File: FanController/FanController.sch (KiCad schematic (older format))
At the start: 16 parts, among them J1 Conn_01x02, J2 Conn_01x02, J3 Conn_01x02, Q1 BTA16, U1 MOC3020, U2 EL817, U3 NodeMCU1.0(ESP-12E)

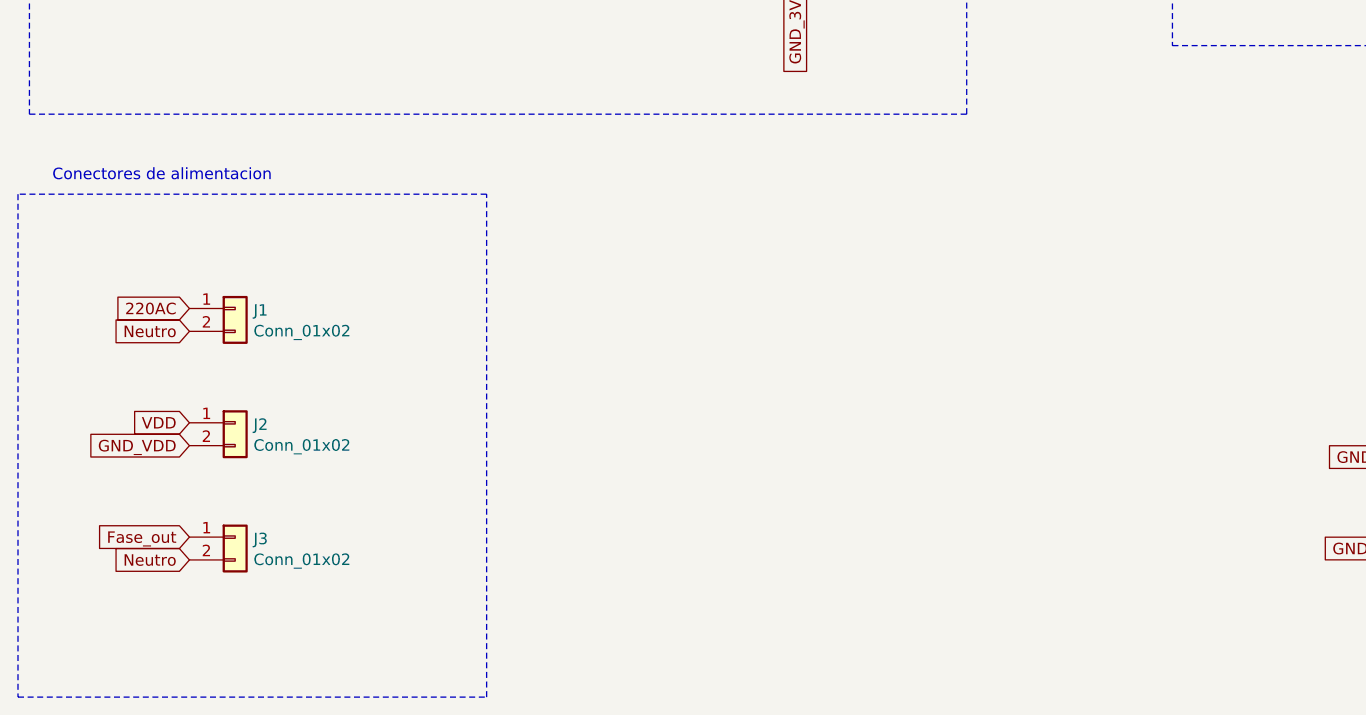
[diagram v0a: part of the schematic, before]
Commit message: added in schematic ASDC suplier for ESP12E.
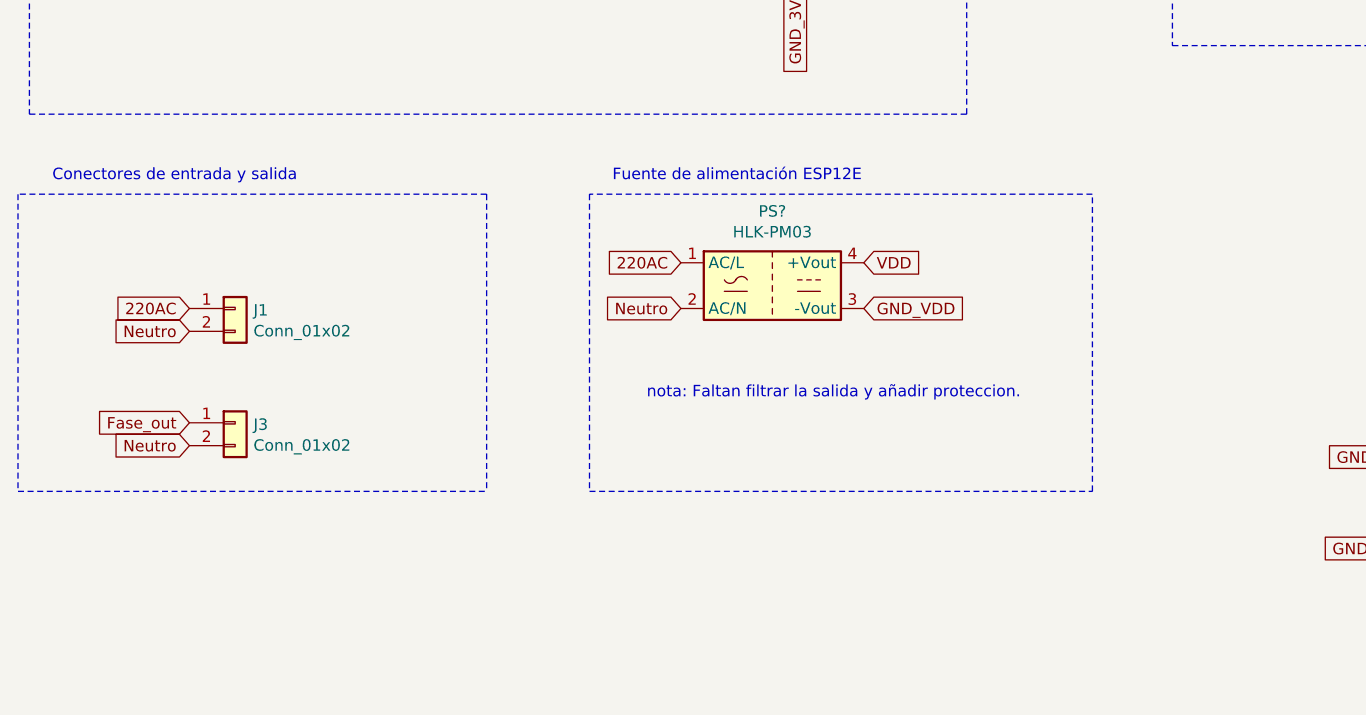
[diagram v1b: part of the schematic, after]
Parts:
- removed J2: Conn_01x02, TerminalBlock_Phoenix:TerminalBlock_Phoenix_MKDS-1,5-2_1x02_P5.00mm_Horizontal, symbol Connector_Generic:Conn_01x02
- added PS?: HLK-PM03, Converter_ACDC:Converter_ACDC_HiLink_HLK-PMxx, symbol Converter_ACDC:HLK-PM03
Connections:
- net 220AC: now also PS?.1 (AC/L)
- net GND_VDD: now also PS?.3 (-Vout)
- net Neutro: now also PS?.2 (AC/N)
- net VDD: now also PS?.4 (+Vout)
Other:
- note added: "Conectores de entrada y salida\n"
- note added: "Fuente de alimentación ESP12E\n"
- note added: "nota: Faltan filtrar la salida y añadir proteccion."
- note removed: "Conectores de alimentacion\n"
- moved on the sheet: J3
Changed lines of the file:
@@
 Comment4 ""
 $EndDescr
-Wire Notes Line
-	1350 4050 1350 6250
 Text Notes 1500 4000 0    50   ~ 0
-Conectores de alimentacion\n
+Conectores de entrada y salida\n
 Text GLabel 2000 1800 0    50   Input ~ 0
 220AC
@@
 L Connector_Generic:Conn_01x02 J3
 U 1 1 5EDAB3AB
-P 2300 5550
-F 0 "J3" H 2380 5542 50  0000 L CNN
-F 1 "Conn_01x02" H 2380 5451 50  0000 L CNN
-F 2 "TerminalBlock_Phoenix:TerminalBlock_Phoenix_MKDS-1,5-2_1x02_P5.00mm_Horizontal" H 2300 5550 50  0001 C CNN
-F 3 "~" H 2300 5550 50  0001 C CNN
-	1    2300 5550
-	1    0    0    -1
-$EndComp
-Text GLabel 2100 5650 0    50   Input ~ 0
+P 2300 5050
+F 0 "J3" H 2380 5042 50  0000 L CNN
+F 1 "Conn_01x02" H 2380 4951 50  0000 L CNN
+F 2 "TerminalBlock_Phoenix:TerminalBlock_Phoenix_MKDS-1,5-2_1x02_P5.00mm_Horizontal" H 2300 5050 50  0001 C CNN
+F 3 "~" H 2300 5050 50  0001 C CNN
+	1    2300 5050
+	1    0    0    -1
+$EndComp
+Text GLabel 2100 5150 0    50   Input ~ 0
 Neutro
-Text GLabel 2100 5550 0    50   Input ~ 0
+Text GLabel 2100 5050 0    50   Input ~ 0
 Fase_out
 $Comp
@@
 NoConn ~ 7500 5000
 NoConn ~ 7500 5100
-$Comp
-L Connector_Generic:Conn_01x02 J2
-U 1 1 5ECAE5DF
-P 2300 5050
-F 0 "J2" H 2380 5042 50  0000 L CNN
-F 1 "Conn_01x02" H 2380 4951 50  0000 L CNN
-F 2 "TerminalBlock_Phoenix:TerminalBlock_Phoenix_MKDS-1,5-2_1x02_P5.00mm_Horizontal" H 2300 5050 50  0001 C CNN
-F 3 "~" H 2300 5050 50  0001 C CNN
-	1    2300 5050
-	1    0    0    -1
-$EndComp
-Text GLabel 2100 5050 0    50   Input ~ 0
+Text GLabel 5050 4350 2    50   Input ~ 0
 VDD
-Text GLabel 2100 5150 0    50   Input ~ 0
+Text GLabel 5050 4550 2    50   Input ~ 0
 GND_VDD
 Text GLabel 7500 5700 0    50   Input ~ 0
@@
 GND_VDD
 Wire Notes Line
-	1350 6250 3400 6250
-Wire Notes Line
-	3400 6250 3400 4050
+	1350 5350 3400 5350
 Wire Notes Line
 	3400 4050 1350 4050
+$Comp
+L Converter_ACDC:HLK-PM03 PS?
+U 1 1 5F2C88CC
+P 4650 4450
+F 0 "PS?" H 4650 4775 50  0000 C CNN
+F 1 "HLK-PM03" H 4650 4684 50  0000 C CNN
+F 2 "Converter_ACDC:Converter_ACDC_HiLink_HLK-PMxx" H 4650 4150 50  0001 C CNN
+F 3 "http://www.hlktech.net/product_detail.php?ProId=59" H 5050 4100 50  0001 C CNN
+	1    4650 4450
+	1    0    0    -1
+$EndComp
+Text GLabel 4250 4350 0    50   Input ~ 0
+220AC
+Text GLabel 4250 4550 0    50   Input ~ 0
+Neutro
+Wire Notes Line
+	3400 4050 3400 5350
+Wire Notes Line
+	3850 4050 3850 5350
+Wire Notes Line
+	3850 5350 6050 5350
+Wire Notes Line
+	6050 5350 6050 4050
+Wire Notes Line
+	6050 4050 3850 4050
+Text Notes 3950 4000 0    50   ~ 0
+Fuente de alimentación ESP12E\n
+Text Notes 4100 4950 0    50   ~ 0
+nota: Faltan filtrar la salida y añadir proteccion.
+Wire Notes Line
+	1350 4050 1350 5350
 $EndSCHEMATC

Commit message: added capacitor network at the output of ACDC
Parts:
- added C1: 10uf, Capacitor_THT:C_Rect_L31.5mm_W13.0mm_P27.50mm_MKS4, symbol Device:CP
- added C2: 22uf, Capacitor_THT:C_Rect_L31.5mm_W13.0mm_P27.50mm_MKS4, symbol Device:CP
- gave numbers to parts that had none: 1
- renumbered J3 to J2
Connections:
- net 220AC: now also R1.1; no longer J1.1 (Pin_1)
- net at F1.1: now also J1.1 (Pin_1); no longer R1.1
- net GND_VDD renamed +3V3
- net +3V3: now also PS1.4 (+Vout), C1.1, C2.1; no longer PS1.3 (-Vout)
- net VDD renamed GND
- net GND: now also PS1.3 (-Vout), C1.2, C2.2; no longer PS1.4 (+Vout)
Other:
- note added: "nota: se podría añadir un fusible para proteger el uC\n\n"
- note removed: "nota: Faltan filtrar la salida y añadir proteccion."
- moved on the sheet: F1, J1, J2, R4, RV1
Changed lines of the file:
@@
 Text Notes 1500 4000 0    50   ~ 0
 Conectores de entrada y salida\n
-Text GLabel 2000 1800 0    50   Input ~ 0
-220AC
-Text GLabel 2000 2250 0    50   Input ~ 0
-Neutro
 $Comp
 L Device:R R1
@@
 L Device:R R4
 U 1 1 5ECD0D61
-P 2150 2450
-F 0 "R4" H 2220 2496 50  0000 L CNN
-F 1 "47K" H 2220 2405 50  0000 L CNN
-F 2 "Resistor_THT:R_Axial_DIN0207_L6.3mm_D2.5mm_P10.16mm_Horizontal" V 2080 2450 50  0001 C CNN
-F 3 "~" H 2150 2450 50  0001 C CNN
-	1    2150 2450
-	1    0    0    -1
-$EndComp
-Wire Wire Line
-	3250 2600 2150 2600
+P 2300 2450
+F 0 "R4" H 2370 2496 50  0000 L CNN
+F 1 "47K" H 2370 2405 50  0000 L CNN
+F 2 "Resistor_THT:R_Axial_DIN0207_L6.3mm_D2.5mm_P10.16mm_Horizontal" V 2230 2450 50  0001 C CNN
+F 3 "~" H 2300 2450 50  0001 C CNN
+	1    2300 2450
+	1    0    0    -1
+$EndComp
 $Comp
 L Device:R R5
@@
 Wire Wire Line
 	4750 3100 4750 2950
-Wire Notes Line
-	1400 1200 1400 3700
-Wire Notes Line
-	1400 3700 5500 3700
-Wire Notes Line
-	5500 3700 5500 1200
-Wire Notes Line
-	5500 1200 1400 1200
-Text Notes 1450 1150 0    50   ~ 0
+Text Notes 1400 950  0    50   ~ 0
 Entrada AC y conversion a sinosoudal de baja tensión\n
 Wire Wire Line
@@
 $EndComp
 Wire Wire Line
-	2000 1800 2150 1800
-Wire Wire Line
 	4600 2650 4750 2650
 Connection ~ 4750 2650
@@
 L Device:Varistor RV1
 U 1 1 5ED798EB
-P 2150 2000
-F 0 "RV1" H 2253 2046 50  0000 L CNN
-F 1 "Varistor" H 2253 1955 50  0000 L CNN
-F 2 "Varistor:RV_Disc_D7mm_W3.4mm_P5mm" V 2080 2000 50  0001 C CNN
-F 3 "~" H 2150 2000 50  0001 C CNN
-	1    2150 2000
-	1    0    0    -1
-$EndComp
-Wire Wire Line
-	2150 1800 2150 1850
+P 2300 1850
+F 0 "RV1" H 2403 1896 50  0000 L CNN
+F 1 "Varistor" H 2403 1805 50  0000 L CNN
+F 2 "Varistor:RV_Disc_D7mm_W3.4mm_P5mm" V 2230 1850 50  0001 C CNN
+F 3 "~" H 2300 1850 50  0001 C CNN
+	1    2300 1850
+	1    0    0    -1
+$EndComp
 $Comp
 L Device:Fuse F1
 U 1 1 5ED7F888
-P 2150 1650
-F 0 "F1" H 2210 1696 50  0000 L CNN
-F 1 "Fuse" H 2210 1605 50  0000 L CNN
-F 2 "Fuse:Fuse_SunFuse-6HP" V 2080 1650 50  0001 C CNN
-F 3 "~" H 2150 1650 50  0001 C CNN
-	1    2150 1650
-	1    0    0    -1
+P 2000 1450
+F 0 "F1" H 2060 1496 50  0000 L CNN
+F 1 "Fuse" H 2060 1405 50  0000 L CNN
+F 2 "Fuse:Fuse_SunFuse-6HP" V 1930 1450 50  0001 C CNN
+F 3 "~" H 2000 1450 50  0001 C CNN
+	1    2000 1450
+	0    -1   -1   0
 $EndComp
 Wire Wire Line
 	3250 2250 3250 2600
-Wire Wire Line
-	2150 1500 2150 1450
-Wire Wire Line
-	2150 1450 2500 1450
 Wire Wire Line
 	2800 1450 3250 1450
@@
 L Connector_Generic:Conn_01x02 J1
 U 1 1 5ED88B7D
-P 2300 4550
-F 0 "J1" H 2380 4542 50  0000 L CNN
-F 1 "Conn_01x02" H 2380 4451 50  0000 L CNN
-F 2 "TerminalBlock_Phoenix:TerminalBlock_Phoenix_MKDS-1,5-2_1x02_P5.00mm_Horizontal" H 2300 4550 50  0001 C CNN
-F 3 "~" H 2300 4550 50  0001 C CNN
-	1    2300 4550
-	1    0    0    -1
-$EndComp
-Text GLabel 2100 4550 0    50   Input ~ 0
-220AC
-Text GLabel 2100 4650 0    50   Input ~ 0
-Neutro
-Wire Wire Line
-	2000 2250 2150 2250
-Wire Wire Line
-	2150 2250 2150 2300
-Wire Wire Line
-	2150 2150 2150 2250
-Connection ~ 2150 2250
+P 1550 2000
+F 0 "J1" H 1630 1992 50  0000 L CNN
+F 1 "Conn_01x02" H 1630 1901 50  0000 L CNN
+F 2 "TerminalBlock_Phoenix:TerminalBlock_Phoenix_MKDS-1,5-2_1x02_P5.00mm_Horizontal" H 1550 2000 50  0001 C CNN
+F 3 "~" H 1550 2000 50  0001 C CNN
+	1    1550 2000
+	-1   0    0    -1
+$EndComp
 $Comp
 L Device:R R3
@@
 Fase_out
 $Comp
-L Connector_Generic:Conn_01x02 J3
+L Connector_Generic:Conn_01x02 J2
 U 1 1 5EDAB3AB
-P 2300 5050
-F 0 "J3" H 2380 5042 50  0000 L CNN
-F 1 "Conn_01x02" H 2380 4951 50  0000 L CNN
-F 2 "TerminalBlock_Phoenix:TerminalBlock_Phoenix_MKDS-1,5-2_1x02_P5.00mm_Horizontal" H 2300 5050 50  0001 C CNN
-F 3 "~" H 2300 5050 50  0001 C CNN
-	1    2300 5050
-	1    0    0    -1
-$EndComp
-Text GLabel 2100 5150 0    50   Input ~ 0
+P 2350 4600
+F 0 "J2" H 2430 4592 50  0000 L CNN
+F 1 "Conn_01x02" H 2430 4501 50  0000 L CNN
+F 2 "TerminalBlock_Phoenix:TerminalBlock_Phoenix_MKDS-1,5-2_1x02_P5.00mm_Horizontal" H 2350 4600 50  0001 C CNN
+F 3 "~" H 2350 4600 50  0001 C CNN
+	1    2350 4600
+	1    0    0    -1
+$EndComp
+Text GLabel 2150 4700 0    50   Input ~ 0
 Neutro
-Text GLabel 2100 5050 0    50   Input ~ 0
+Text GLabel 2150 4600 0    50   Input ~ 0
 Fase_out
 $Comp
@@
 NoConn ~ 7500 5000
 NoConn ~ 7500 5100
-Text GLabel 5050 4350 2    50   Input ~ 0
-VDD
-Text GLabel 5050 4550 2    50   Input ~ 0
-GND_VDD
-Text GLabel 7500 5700 0    50   Input ~ 0
-VDD
-Text GLabel 7500 5600 0    50   Input ~ 0
-GND_VDD
 Wire Notes Line
 	1350 5350 3400 5350
@@
 	3400 4050 1350 4050
 $Comp
-L Converter_ACDC:HLK-PM03 PS?
+L Converter_ACDC:HLK-PM03 PS1
 U 1 1 5F2C88CC
 P 4650 4450
-F 0 "PS?" H 4650 4775 50  0000 C CNN
+F 0 "PS1" H 4650 4775 50  0000 C CNN
 F 1 "HLK-PM03" H 4650 4684 50  0000 C CNN
 F 2 "Converter_ACDC:Converter_ACDC_HiLink_HLK-PMxx" H 4650 4150 50  0001 C CNN
@@
 	1    0    0    -1
 $EndComp
+Wire Notes Line
+	3400 4050 3400 5350
+Wire Notes Line
+	3850 4050 3850 5350
+Wire Notes Line
+	3850 5350 6050 5350
+Wire Notes Line
+	6050 5350 6050 4050
+Wire Notes Line
+	6050 4050 3850 4050
+Text Notes 3950 4000 0    50   ~ 0
+Fuente de alimentación ESP12E\n
+Text Notes 3950 5300 0    50   ~ 0
+nota: se podría añadir un fusible para proteger el uC\n\n
+Wire Notes Line
+	1350 4050 1350 5350
+Wire Wire Line
+	1750 2000 1750 1450
+Wire Wire Line
+	1750 1450 1850 1450
+Wire Wire Line
+	3250 2600 2300 2600
+Wire Wire Line
+	1750 2100 1750 2200
+Wire Wire Line
+	2150 1450 2300 1450
+Wire Wire Line
+	2300 1700 2300 1450
+Connection ~ 2300 1450
+Wire Wire Line
+	2300 1450 2500 1450
+Wire Wire Line
+	2300 2000 2300 2200
+Wire Wire Line
+	1750 2200 2300 2200
+Connection ~ 2300 2200
+Wire Wire Line
+	2300 2200 2300 2300
+Wire Notes Line
+	950  1050 5500 1050
+Wire Notes Line
+	950  3700 5500 3700
+Text GLabel 2300 1450 1    50   Input ~ 0
+220AC
+Text GLabel 2300 2200 2    50   Input ~ 0
+Neutro
+Wire Notes Line
+	950  1050 950  3700
+Wire Notes Line
+	5500 1050 5500 3700
+$Comp
+L Device:CP C1
+U 1 1 5F2EE584
+P 5300 4450
+F 0 "C1" H 5418 4496 50  0000 L CNN
+F 1 "10uf" H 5418 4405 50  0000 L CNN
+F 2 "Capacitor_THT:C_Rect_L31.5mm_W13.0mm_P27.50mm_MKS4" H 5338 4300 50  0001 C CNN
+F 3 "~" H 5300 4450 50  0001 C CNN
+	1    5300 4450
+	1    0    0    -1
+$EndComp
+$Comp
+L Device:CP C2
+U 1 1 5F2F294A
+P 5750 4450
+F 0 "C2" H 5868 4496 50  0000 L CNN
+F 1 "22uf" H 5868 4405 50  0000 L CNN
+F 2 "Capacitor_THT:C_Rect_L31.5mm_W13.0mm_P27.50mm_MKS4" H 5788 4300 50  0001 C CNN
+F 3 "~" H 5750 4450 50  0001 C CNN
+	1    5750 4450
+	1    0    0    -1
+$EndComp
+Wire Wire Line
+	5050 4350 5050 4300
+Wire Wire Line
+	5050 4300 5300 4300
+Wire Wire Line
+	5300 4300 5750 4300
+Connection ~ 5300 4300
+Wire Wire Line
+	5050 4550 5050 4600
+Wire Wire Line
+	5050 4600 5300 4600
+Wire Wire Line
+	5300 4600 5750 4600
+Connection ~ 5300 4600
+$Comp
+L power:+3V3 #PWR0101
+U 1 1 5F2F851E
+P 5750 4300
+F 0 "#PWR0101" H 5750 4150 50  0001 C CNN
+F 1 "+3V3" H 5765 4473 50  0000 C CNN
+F 2 "" H 5750 4300 50  0001 C CNN
+F 3 "" H 5750 4300 50  0001 C CNN
+	1    5750 4300
+	1    0    0    -1
+$EndComp
+Connection ~ 5750 4300
+$Comp
+L power:GND #PWR0102
+U 1 1 5F2FB000
+P 5750 4600
+F 0 "#PWR0102" H 5750 4350 50  0001 C CNN
+F 1 "GND" H 5755 4427 50  0000 C CNN
+F 2 "" H 5750 4600 50  0001 C CNN
+F 3 "" H 5750 4600 50  0001 C CNN
+	1    5750 4600
+	1    0    0    -1
+$EndComp
+Connection ~ 5750 4600
+$Comp
+L power:GND #PWR0103
+U 1 1 5F2FD8F0
+P 7500 5750
+F 0 "#PWR0103" H 7500 5500 50  0001 C CNN
+F 1 "GND" H 7505 5577 50  0000 C CNN
+F 2 "" H 7500 5750 50  0001 C CNN
+F 3 "" H 7500 5750 50  0001 C CNN
+	1    7500 5750
+	1    0    0    -1
+$EndComp
+Wire Wire Line
+	7500 5750 7500 5700
+$Comp
+L power:+3V3 #PWR0104
+U 1 1 5F2FE6E2
+P 7300 5600
+F 0 "#PWR0104" H 7300 5450 50  0001 C CNN
+F 1 "+3V3" H 7315 5773 50  0000 C CNN
+F 2 "" H 7300 5600 50  0001 C CNN
+F 3 "" H 7300 5600 50  0001 C CNN
+	1    7300 5600
+	1    0    0    -1
+$EndComp
+Wire Wire Line
+	7300 5600 7500 5600
 Text GLabel 4250 4350 0    50   Input ~ 0
 220AC
 Text GLabel 4250 4550 0    50   Input ~ 0
 Neutro
-Wire Notes Line
-	3400 4050 3400 5350
-Wire Notes Line
-	3850 4050 3850 5350
-Wire Notes Line
-	3850 5350 6050 5350
-Wire Notes Line
-	6050 5350 6050 4050
-Wire Notes Line
-	6050 4050 3850 4050
-Text Notes 3950 4000 0    50   ~ 0
-Fuente de alimentación ESP12E\n
-Text Notes 4100 4950 0    50   ~ 0
-nota: Faltan filtrar la salida y añadir proteccion.
-Wire Notes Line
-	1350 4050 1350 5350
 $EndSCHEMATC

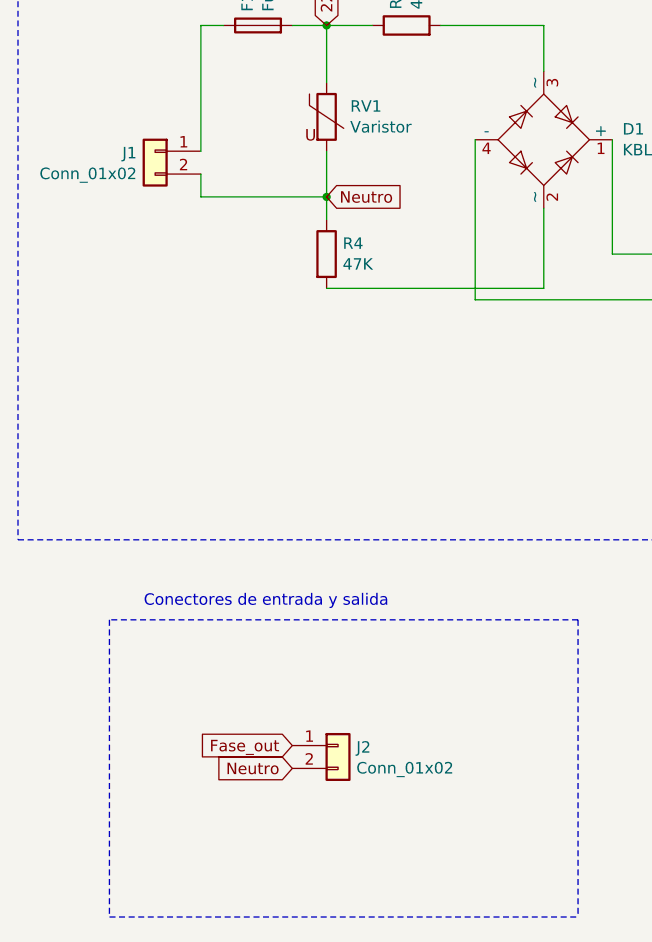
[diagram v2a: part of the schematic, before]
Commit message: renamed conector J1 adn J2
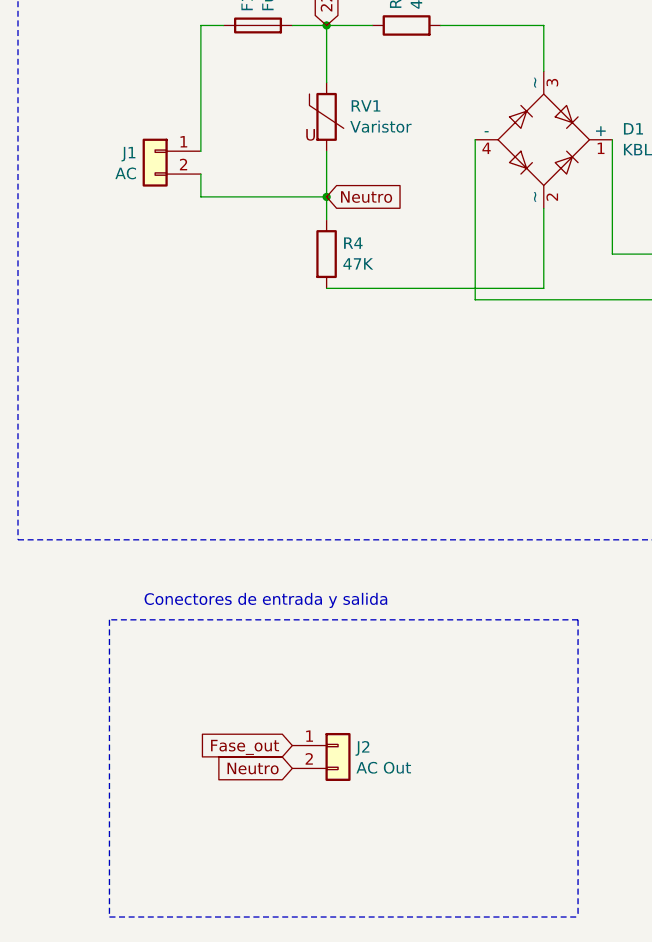
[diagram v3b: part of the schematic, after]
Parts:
- J1: value Conn_01x02 -> AC
- J2: value Conn_01x02 -> AC Out
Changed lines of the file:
@@
 P 1550 2000
 F 0 "J1" H 1630 1992 50  0000 L CNN
-F 1 "Conn_01x02" H 1630 1901 50  0000 L CNN
+F 1 "AC" H 1630 1901 50  0000 L CNN
 F 2 "TerminalBlock_Phoenix:TerminalBlock_Phoenix_MKDS-1,5-2_1x02_P5.00mm_Horizontal" H 1550 2000 50  0001 C CNN
 F 3 "~" H 1550 2000 50  0001 C CNN
@@
 P 2350 4600
 F 0 "J2" H 2430 4592 50  0000 L CNN
-F 1 "Conn_01x02" H 2430 4501 50  0000 L CNN
+F 1 "AC Out" H 2430 4501 50  0000 L CNN
 F 2 "TerminalBlock_Phoenix:TerminalBlock_Phoenix_MKDS-1,5-2_1x02_P5.00mm_Horizontal" H 2350 4600 50  0001 C CNN
 F 3 "~" H 2350 4600 50  0001 C CNN
